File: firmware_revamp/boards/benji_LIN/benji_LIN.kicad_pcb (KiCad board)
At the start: 2 copper layers, 35 parts, among them J1 CONN_02X03, J2 Conn_01x11, J3 Conn_01x11, J4 CONN_01X03, SW1 SW_Push_SPST_NO, U1 MCP2561-E_SN, U2 ATMEGA16M1, U3 TLIN1021DRQ1, Y1 Crystal_SMD

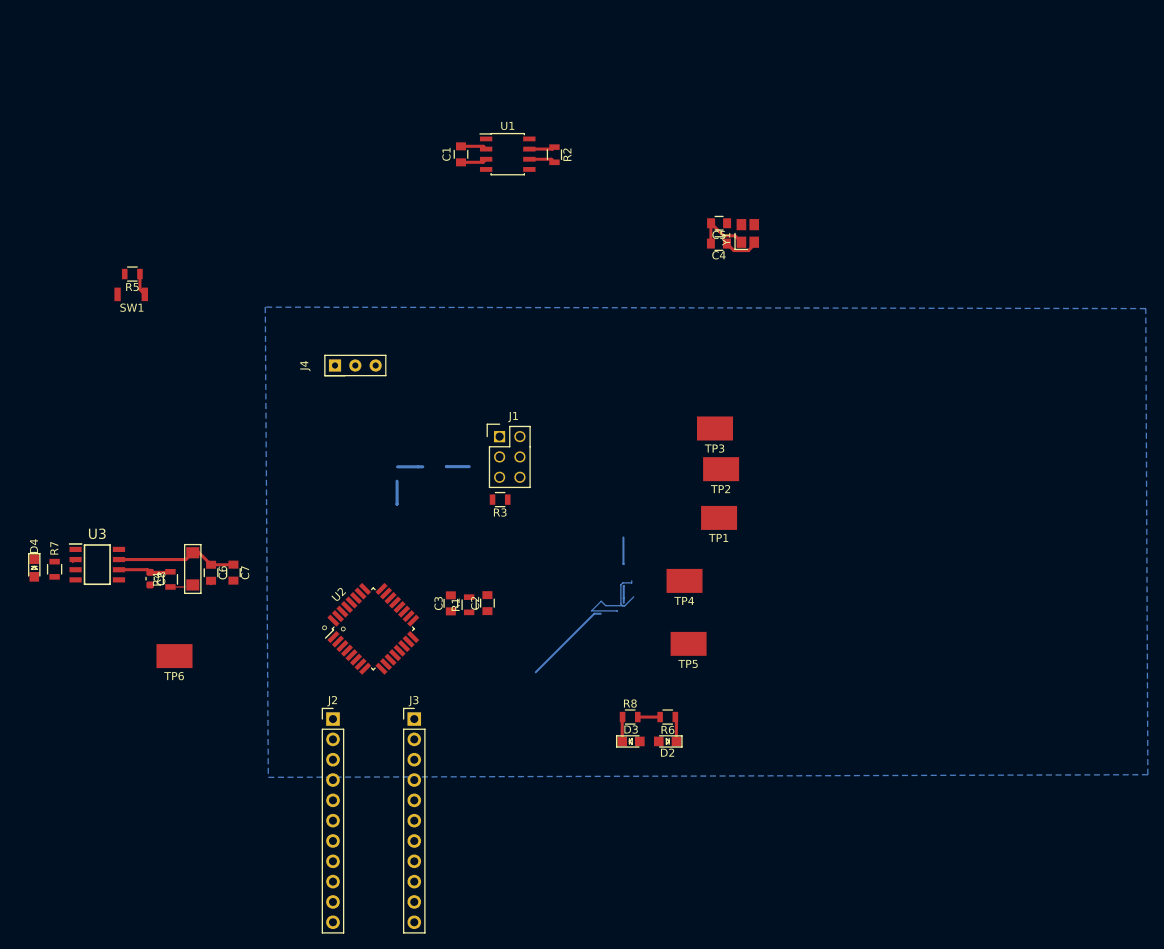
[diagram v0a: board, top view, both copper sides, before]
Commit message: Reworked with DXF
TODO: connect headers, add vias to ground, add silkscreens
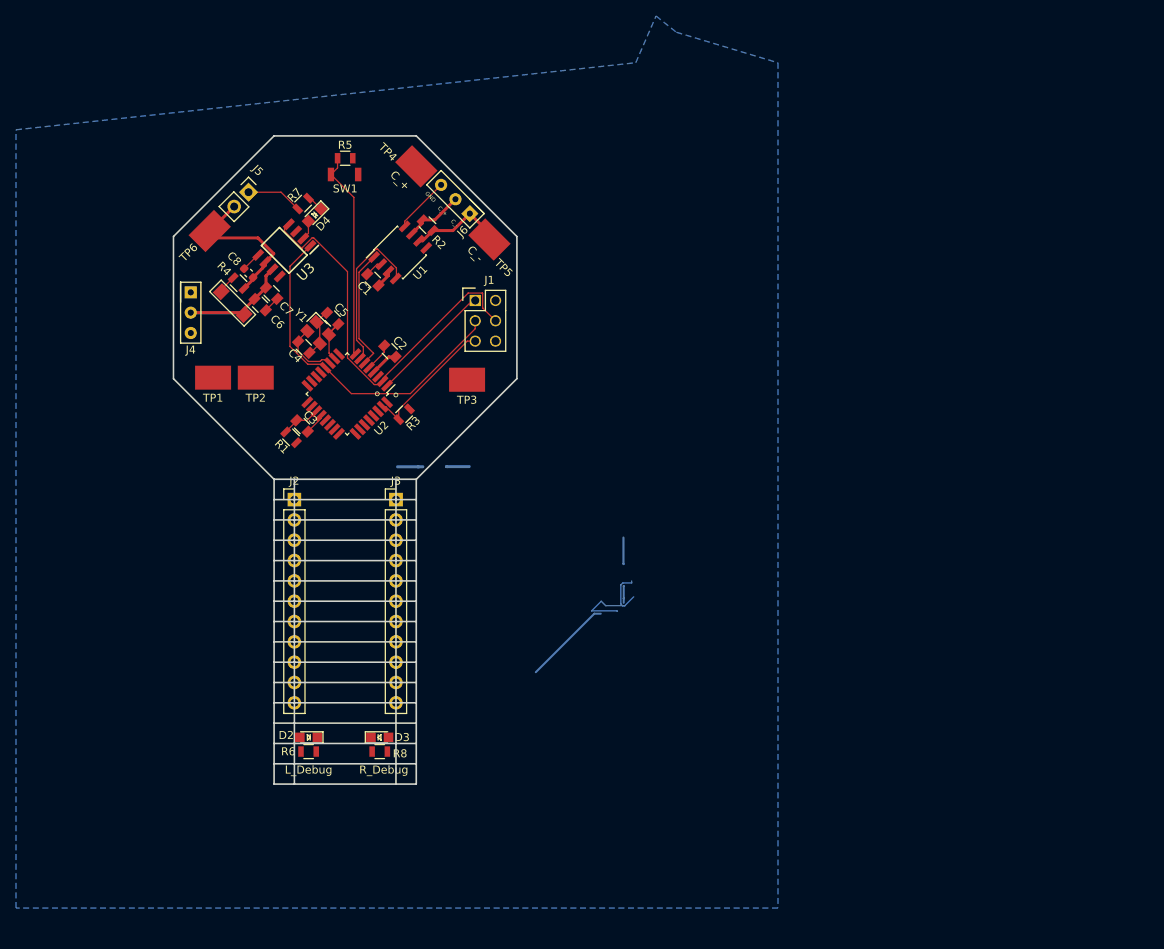
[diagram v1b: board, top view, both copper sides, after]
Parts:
- added J5: CONN_01x02, Connector_PinHeader_2.54mm:PinHeader_1x02_P2.54mm_Vertical, F.Cu at (96.1, 61.9)
- added J6: CONN_01X03, footprints:PinHeader_1x03_P2.54mm_Vertical, F.Cu at (123.8, 64.6)
- moved TP1 65.6 mm to (91.7, 85.1)
- moved TP4 61.7 mm to (117.1, 58.7), turned to 315 degrees
- moved TP2 59.3 mm to (97.0, 85.1)
- moved D4 56.3 mm to (104.4, 64.8), turned to 225 degrees
- moved TP5 56.3 mm to (126.2, 67.8), turned to 315 degrees
- moved R7 55.3 mm to (102.9, 63.3), turned to 225 degrees
- moved Y1 55.1 mm to (104.8, 79.5), turned to 315 degrees
- moved C4 53.5 mm to (103.0, 81.3), turned to 315 degrees
- moved TP6 53.3 mm to (91.3, 66.8), turned to 45 degrees
- moved C5 49.7 mm to (106.6, 77.7), turned to 135 degrees
- moved U3 45.7 mm to (100.6, 69.2), turned to 225 degrees
- moved R6 45.1 mm to (103.6, 131.8)
- moved D2 44.9 mm to (103.6, 130.0)
- moved C8 40.1 mm to (96.1, 72.0), turned to 135 degrees
- moved R4 38.0 mm to (94.9, 73.3), turned to 315 degrees
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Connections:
- J2 pad 2: GND -> /12V
- J2 pad 3: Net-(J2-Pad3) -> GND
- J3 pad 2: GND -> /12V
- J3 pad 3: Net-(J3-Pad3) -> GND
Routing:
- net /MOSI: track 0.00 -> 50.4 mm
- net /RXLIN: track 0.00 -> 43.6 mm
- net GND: track 28.1 -> 70.0 mm
- net Net-(J2-Pad9): track 25.6 -> 0.00 mm
- net Net-(R5-Pad1): track 2.79 -> 26.1 mm
- net /CAN_RX: track 0.00 -> 20.1 mm
- net /RESET: track 0.00 -> 17.0 mm
- net /MISO: track 0.00 -> 15.4 mm
- net /CAN_TX: track 0.00 -> 15.3 mm
- net /LIN_BUS: track 6.70 -> 19.4 mm
- net /CAN_-: track 3.30 -> 12.0 mm
- net Net-(C5-Pad1): track 0.24 -> 7.44 mm
- net Net-(C3-Pad1): track 0.00 -> 5.08 mm
- net /VIN: track 15.7 -> 20.5 mm
- net /CAN_+: track 3.25 -> 7.49 mm
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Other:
- board outline added: 42.9 x 81 mm
- board text added: "C_+"
- board text added: "C_-"
- board text added: "GND"
- board text added: "L_Debug"
- board text added: "R_Debug"

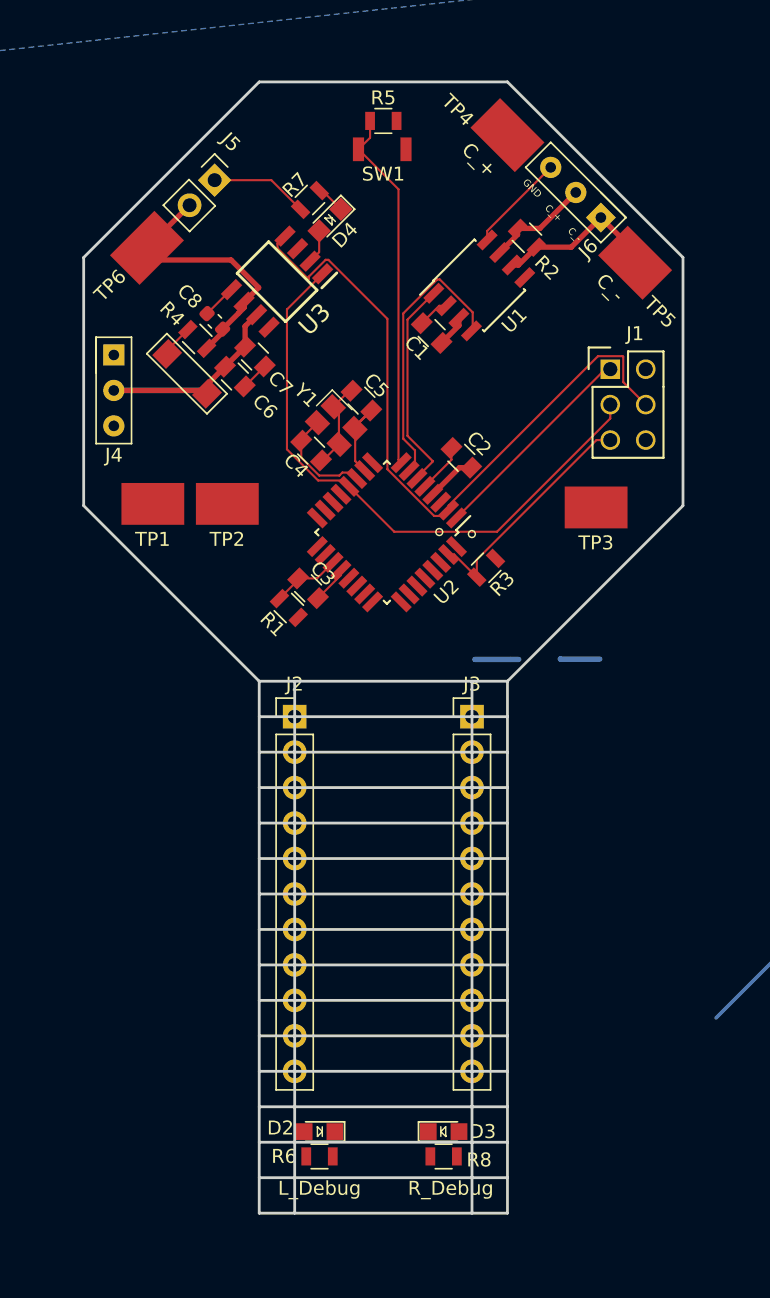
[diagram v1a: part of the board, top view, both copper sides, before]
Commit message: Amended and finished up layout
assigned pins to headers, changed diode to led on LIN transciever
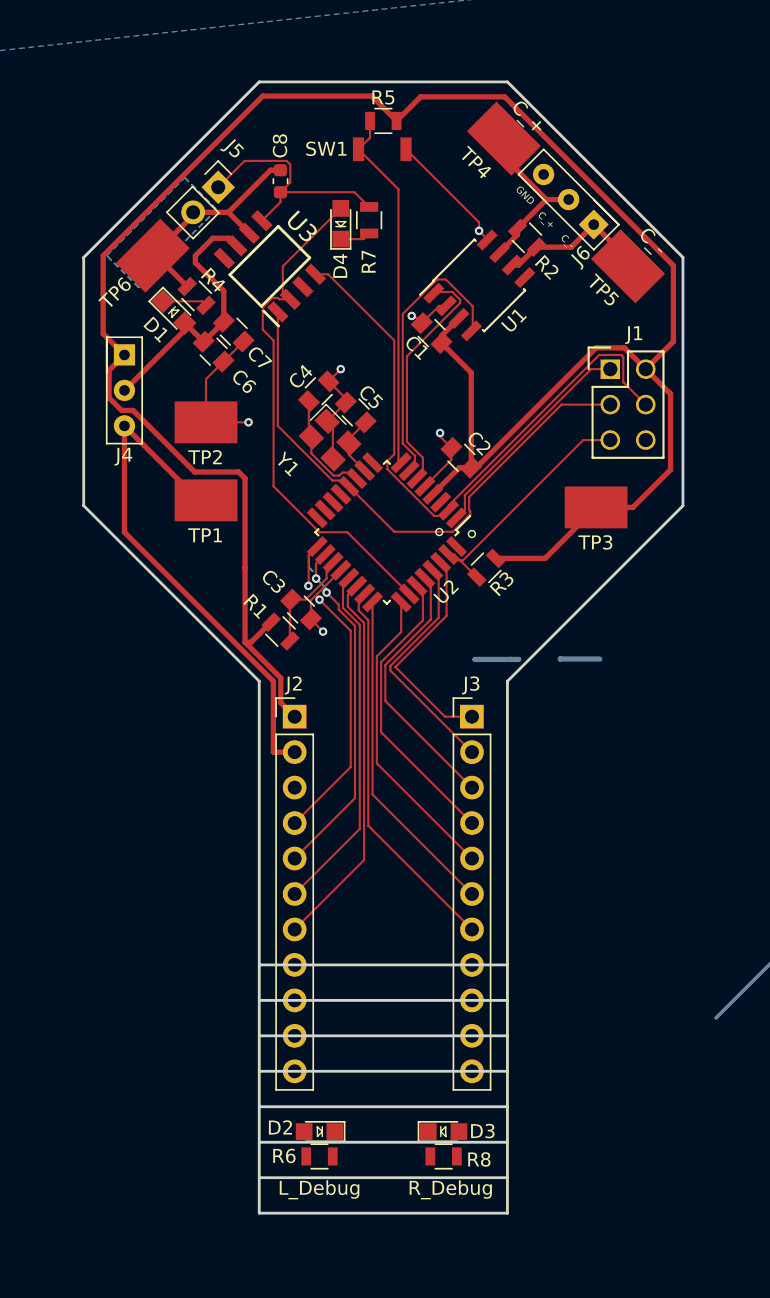
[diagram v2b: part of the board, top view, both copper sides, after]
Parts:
- D1: value Diode_600V_1A_SM -> LED_0805; footprint footprints:Diode_600V_1A_SM -> footprints:LED_0805_OEM
- moved C8 11.1 mm to (100.8, 62.0), turned to 270 degrees
- moved D1 6.30 mm to (93.2, 71.4), turned to 315 degrees
- moved TP2 6.04 mm to (95.5, 79.2)
- moved R7 4.48 mm to (107.2, 64.8), turned to 90 degrees
- moved C4 4.29 mm to (103.6, 77.0), turned to 45 degrees
- moved TP1 3.82 mm to (95.5, 84.8)
- moved R4 3.08 mm to (94.8, 70.2), turned to 135 degrees
- moved C6 2.34 mm to (96.0, 74.2)
- moved C7 2.34 mm to (97.5, 72.8)
- moved R1 1.79 mm to (100.8, 94.2), turned to 315 degrees
- moved C3 1.61 mm to (102.3, 92.7)
- moved U3 1.22 mm to (100.1, 68.1), turned to 135 degrees
- moved Y1 1.13 mm to (104.4, 80.5)
- moved C5 0.94 mm to (106.2, 78.5)
- moved D4 0.82 mm to (105.2, 65.0), turned to 90 degrees
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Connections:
- D1 pad 1: /VIN -> Net-(D1-Pad1)
- D1 pad 2: Net-(D1-Pad2) -> /VIN
- J2 pad 4: Net-(J2-Pad4) -> /GPIO_1
- J2 pad 5: Net-(J2-Pad5) -> /GPIO_2
- J2 pad 6: Net-(J2-Pad6) -> /GPIO_3
- J2 pad 7: Net-(J2-Pad7) -> /GPIO_4
- J3 pad 1: VCC -> /GPIO_5
- J3 pad 2: /12V -> /GPIO_6
- J3 pad 3: GND -> /GPIO_7
- J3 pad 4: Net-(J3-Pad4) -> /GPIO_8
- J3 pad 5: Net-(J3-Pad5) -> /GPIO_9
- J3 pad 6: Net-(J3-Pad6) -> /GPIO_10
- J3 pad 7: Net-(J3-Pad7) -> /GPIO_11
- R4 pad 1: Net-(D1-Pad2) -> Net-(D1-Pad1)
- U2 pad 17: Net-(U2-Pad17) -> /GPIO_1
- U2 pad 18: Net-(U2-Pad18) -> /GPIO_2
- U2 pad 21: Net-(U2-Pad21) -> /GPIO_3
- U2 pad 22: Net-(U2-Pad22) -> /GPIO_4
- U2 pad 23: Net-(U2-Pad23) -> /GPIO_11
- U2 pad 24: Net-(U2-Pad24) -> /GPIO_10
- U2 pad 25: Net-(U2-Pad25) -> /GPIO_9
- U2 pad 27: Net-(U2-Pad27) -> /GPIO_8
- U2 pad 28: Net-(U2-Pad28) -> /GPIO_7
- U2 pad 29: Net-(U2-Pad29) -> /GPIO_6
- U2 pad 30: Net-(U2-Pad30) -> /GPIO_5
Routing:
- net VCC: track 5.82 -> 160.1 mm
- net /12V: track 0.00 -> 37.4 mm
- net /ENABLE: track 2.69 -> 36.8 mm
- net /GPIO_11: track 0.00 -> 27.6 mm
- net /GPIO_4: track 0.00 -> 27.4 mm
- net GND: track 70.0 -> 95.4 mm, vias 0 -> 6
- net /GPIO_3: track 0.00 -> 25.2 mm
- net /GPIO_2: track 0.00 -> 24.7 mm, vias 0 -> 2
- net /GPIO_10: track 0.00 -> 23.9 mm
- net /GPIO_1: track 0.00 -> 22.1 mm, vias 0 -> 2
- net /GPIO_9: track 0.00 -> 21.9 mm
- net /GPIO_8: track 0.00 -> 21.1 mm
- net /GPIO_7: track 0.00 -> 19.1 mm
- net /GPIO_6: track 0.00 -> 17.1 mm
- net /GPIO_5: track 0.00 -> 16.2 mm
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- added copper zone on B.Cu, net /LIN_BUS
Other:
- outline, holes or cut-outs redrawn

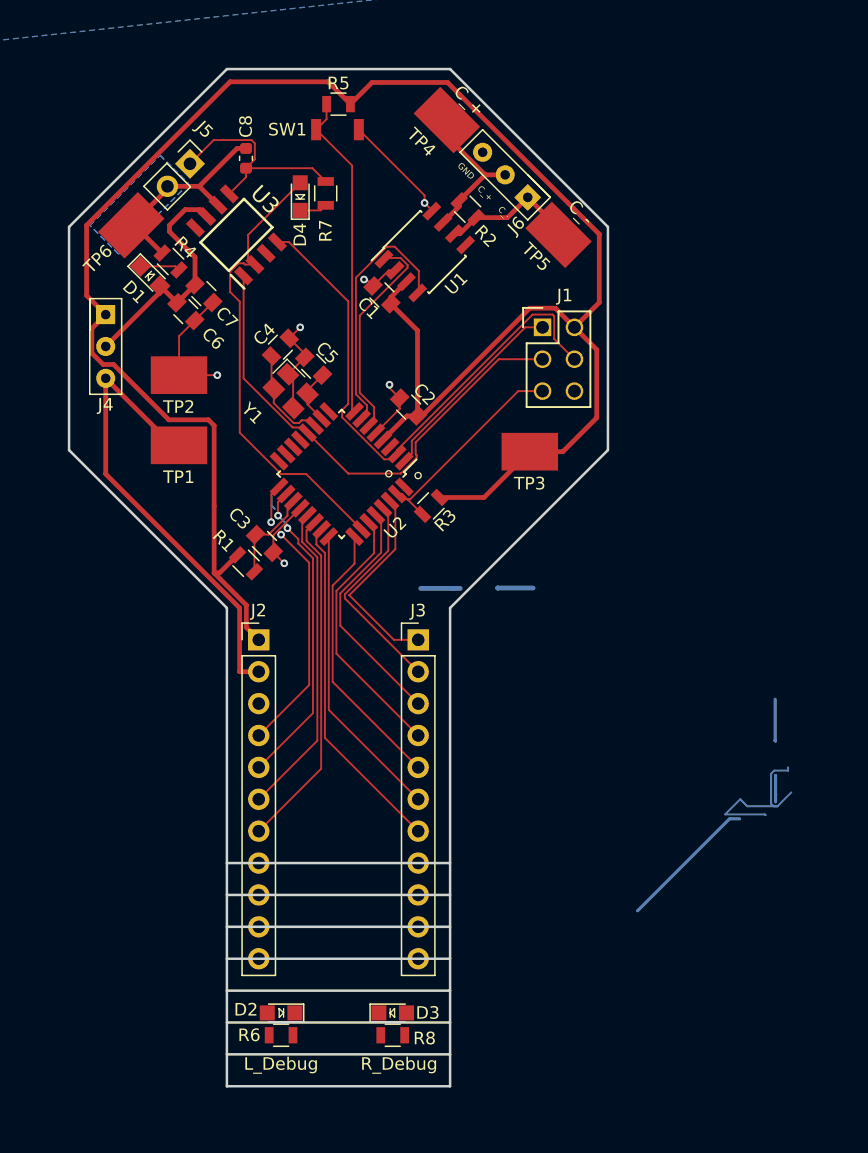
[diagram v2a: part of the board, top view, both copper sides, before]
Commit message: Fixed vias, pins, rearranged debug lEDs
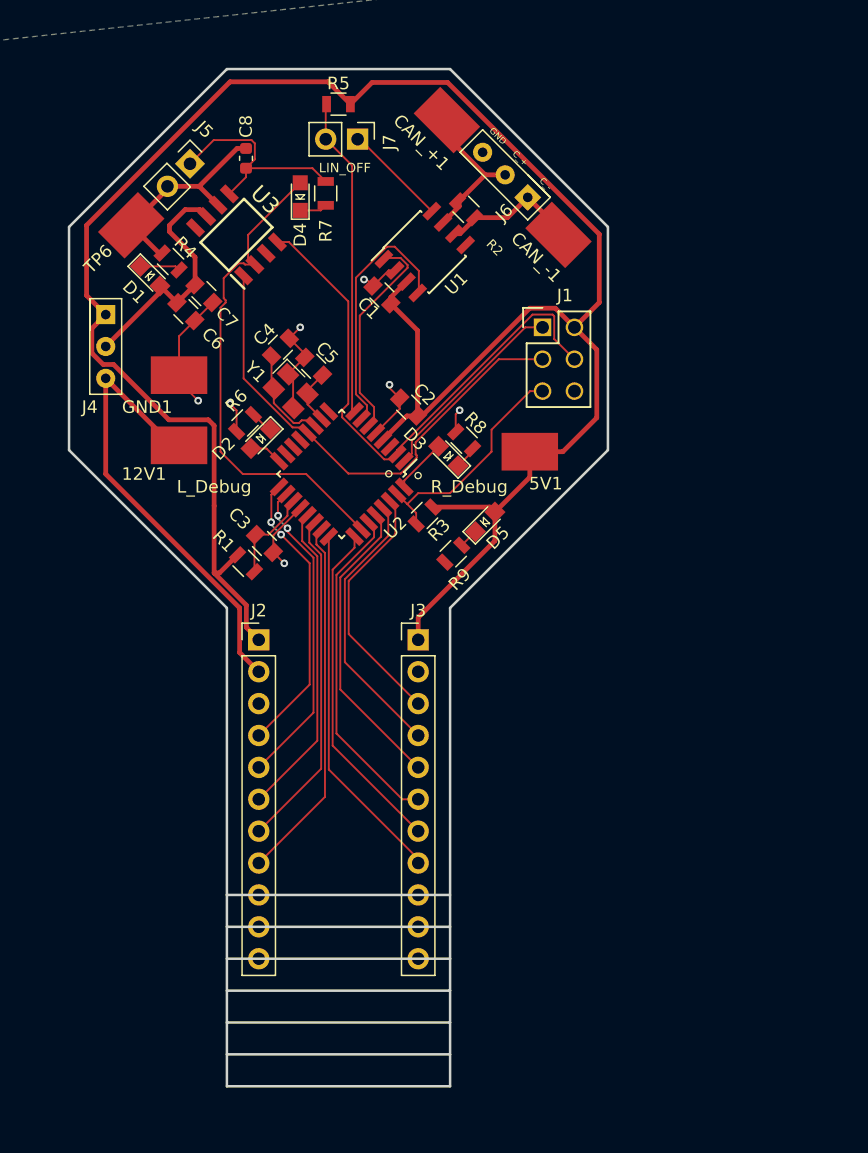
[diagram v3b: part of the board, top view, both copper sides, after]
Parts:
- removed SW1: SW_Push_SPST_NO, footprints:SW_B3U-1000P_4.2x1.7mm
- added D5: LED_0805_Amber, footprints:LED_0805_OEM, F.Cu at (119.9, 90.9)
- added J7: CONN_01x02, Connector_PinHeader_2.54mm:PinHeader_1x02_P2.54mm_Vertical, F.Cu at (109.7, 60.5)
- added R9: R_1K, footprints:R_0805_OEM, F.Cu at (117.3, 93.5)
- moved R6 48.9 mm to (100.8, 83.1), turned to 225 degrees
- moved R8 47.7 mm to (118.2, 84.4), turned to 135 degrees
- moved D2 45.8 mm to (102.0, 84.3), turned to 225 degrees
- moved D3 44.6 mm to (117.0, 85.7), turned to 135 degrees
- moved R3 0.92 mm to (115.1, 90.4)
- moved R2 0.13 mm to (118.4, 66.0)
- renumbered TP1 to 12V1, TP3 to 5V1, TP4 to CAN_+1, TP5 to CAN_-1, TP2 to GND1
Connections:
- J2 pad 8: Net-(J2-Pad8) -> /GPIO_5
- J3 pad 1: /GPIO_5 -> VCC
- J3 pad 2: /GPIO_6 -> GND
- J3 pad 3: /GPIO_7 -> /GPIO_6
- J3 pad 4: /GPIO_8 -> /GPIO_7
- J3 pad 5: /GPIO_9 -> /GPIO_8
- J3 pad 6: /GPIO_10 -> /GPIO_9
- J3 pad 7: /GPIO_11 -> /GPIO_10
- J3 pad 8: Net-(J3-Pad8) -> /GPIO_11
- U2 pad 16: Net-(U2-Pad16) -> /LEFT_DEBUG
- U2 pad 23: /GPIO_11 -> /GPIO_5
- U2 pad 24: /GPIO_10 -> /GPIO_11
- U2 pad 25: /GPIO_9 -> /GPIO_10
- U2 pad 27: /GPIO_8 -> /GPIO_9
- U2 pad 28: /GPIO_7 -> /GPIO_8
- U2 pad 29: /GPIO_6 -> /GPIO_7
- U2 pad 30: /GPIO_5 -> /GPIO_6
- U2 pad 32: Net-(U2-Pad32) -> /RIGHT_DEBUG
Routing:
- net GND: track 95.4 -> 61.7 mm, vias 6 -> 7
- net VCC: track 160.1 -> 175.2 mm
- net /GPIO_5: track 16.2 -> 29.1 mm
- net /GPIO_9: track 21.9 -> 26.9 mm
- net /RIGHT_DEBUG: track 0.00 -> 4.37 mm
- net /GPIO_10: track 23.9 -> 27.0 mm
- net /GPIO_6: track 17.1 -> 20.1 mm
- net /GPIO_8: track 21.1 -> 24.2 mm
- net /GPIO_7: track 19.1 -> 22.1 mm
- net /LEFT_DEBUG: track 0.00 -> 2.65 mm
- net /ENABLE: track 36.8 -> 39.3 mm
- net Net-(D3-Pad1): track 0.00 -> 1.84 mm
- net Net-(D2-Pad1): track 0.20 -> 1.84 mm
- net Net-(D5-Pad1): track 0.00 -> 1.54 mm
- net /GPIO_1: track 22.1 -> 23.4 mm
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- removed copper zone on B.Cu, net /LIN_BUS
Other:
- outline, holes or cut-outs redrawn
- board text added: "LIN_OFF"
